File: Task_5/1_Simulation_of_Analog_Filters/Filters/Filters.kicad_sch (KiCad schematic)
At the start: 10 parts

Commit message: Work on 5.1
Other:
- note added: ".param R_HP=900*pI .param C_HP=1/(8100000*pI*pI)"
- note added: ".param R_LP=300*pI .param C_LP=1/(900000*pI*pI)"
- note added: ".param pI=3.14159 .param f_LP=1500 .param f_HP=4500 .param L=0.1"
- note added: "R_HP = 2*pI*L*f_LP C_HP = 1/(2*pI*R_HP*f_HP)"
- note added: "R_LP = 2*pI*L*f_LP C_LP = 1/(2*pI*R_LP*f_LP)"
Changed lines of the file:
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@@
+		)
+	)
+	(text "R_HP = 2*pI*L*f_LP\nC_HP = 1/(2*pI*R_HP*f_HP)"
+		(exclude_from_sim no)
+		(at 215.646 147.828 0)
+		(effects
+			(font
+				(size 1.27 1.27)
+			)
+		)
+	)
+	(text "R_LP = 2*pI*L*f_LP\nC_LP = 1/(2*pI*R_LP*f_LP)"
+		(exclude_from_sim no)
+		(at 139.7 147.32 0)
+		(effects
+			(font
+				(size 1.27 1.27)
+			)
 		)
 	)
@@
 		(exclude_from_sim no)
 		(at 139.7 44.45 0)
+		(effects
+			(font
+				(size 1.27 1.27)
+			)
+		)
+	)
+	(text ".param R_LP=300*pI\n.param C_LP=1/(900000*pI*pI)"
+		(exclude_from_sim no)
+		(at 139.446 156.464 0)
+		(effects
+			(font
+				(size 1.27 1.27)
+			)
+		)
+	)
+	(text ".param pI=3.14159\n.param f_LP=1500\n.param f_HP=4500\n.param L=0.1"
+		(exclude_from_sim no)
+		(at 261.874 83.058 0)
+		(effects
+			(font
+				(size 1.27 1.27)
+			)
+		)
+	)
+	(text ".param R_HP=900*pI\n.param C_HP=1/(8100000*pI*pI)"
+		(exclude_from_sim no)
+		(at 216.154 155.194 0)
 		(effects
 			(font
@@
 			)
 		)
-		(property "Sim.Params" "dc=0 ampl=1 f=1k ac=1"
+		(property "Sim.Params" "dc=0 ampl=1 f=5k ac=1"
 			(at 67.31 116.7101 0)
 			(effects

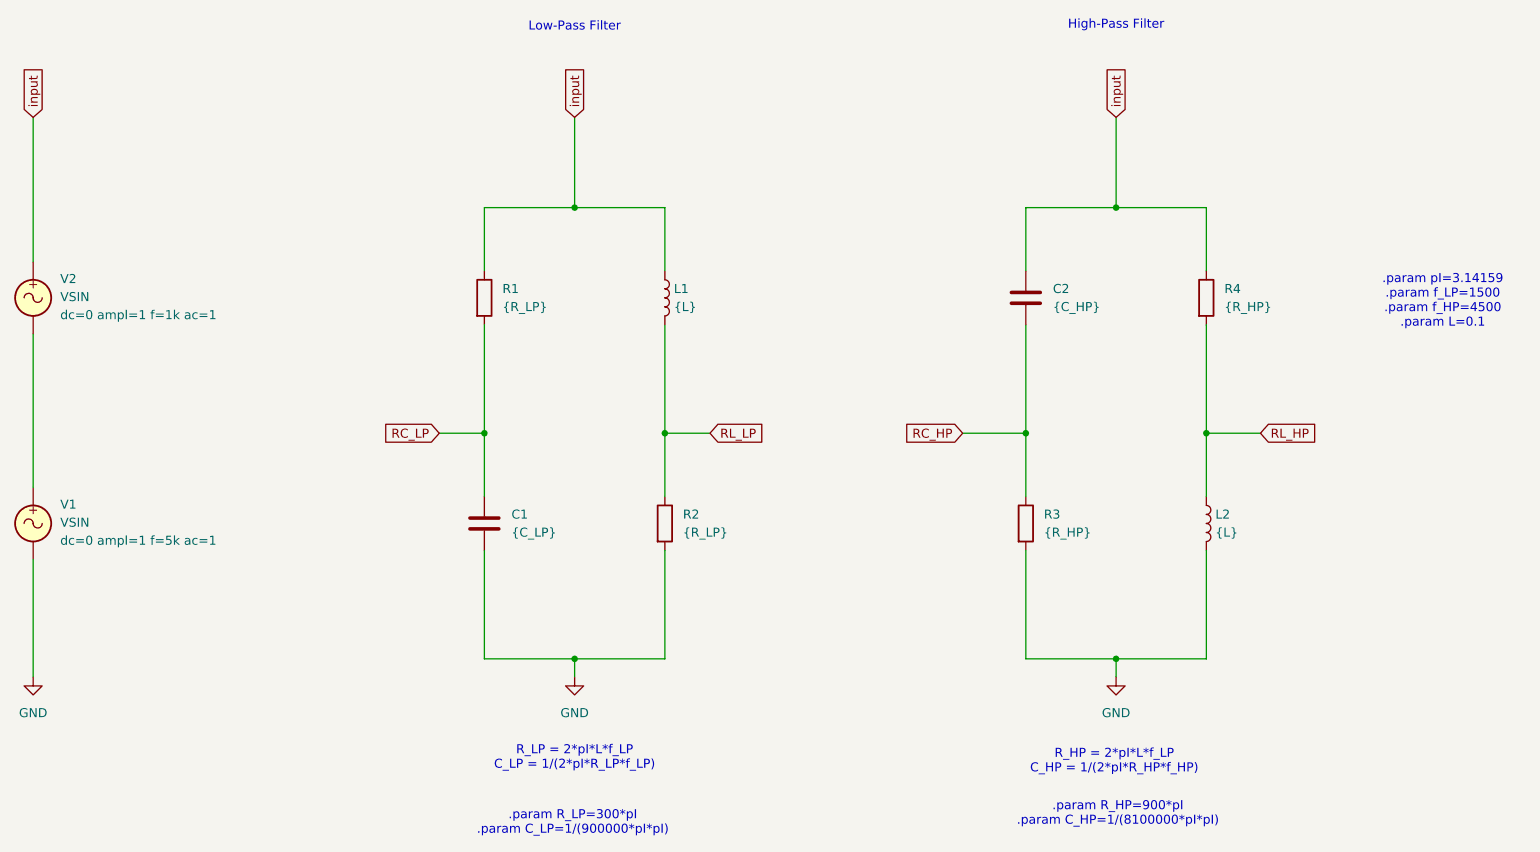
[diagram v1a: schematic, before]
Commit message: Ableiten von Bildern und daten für 5.1 und 5.3
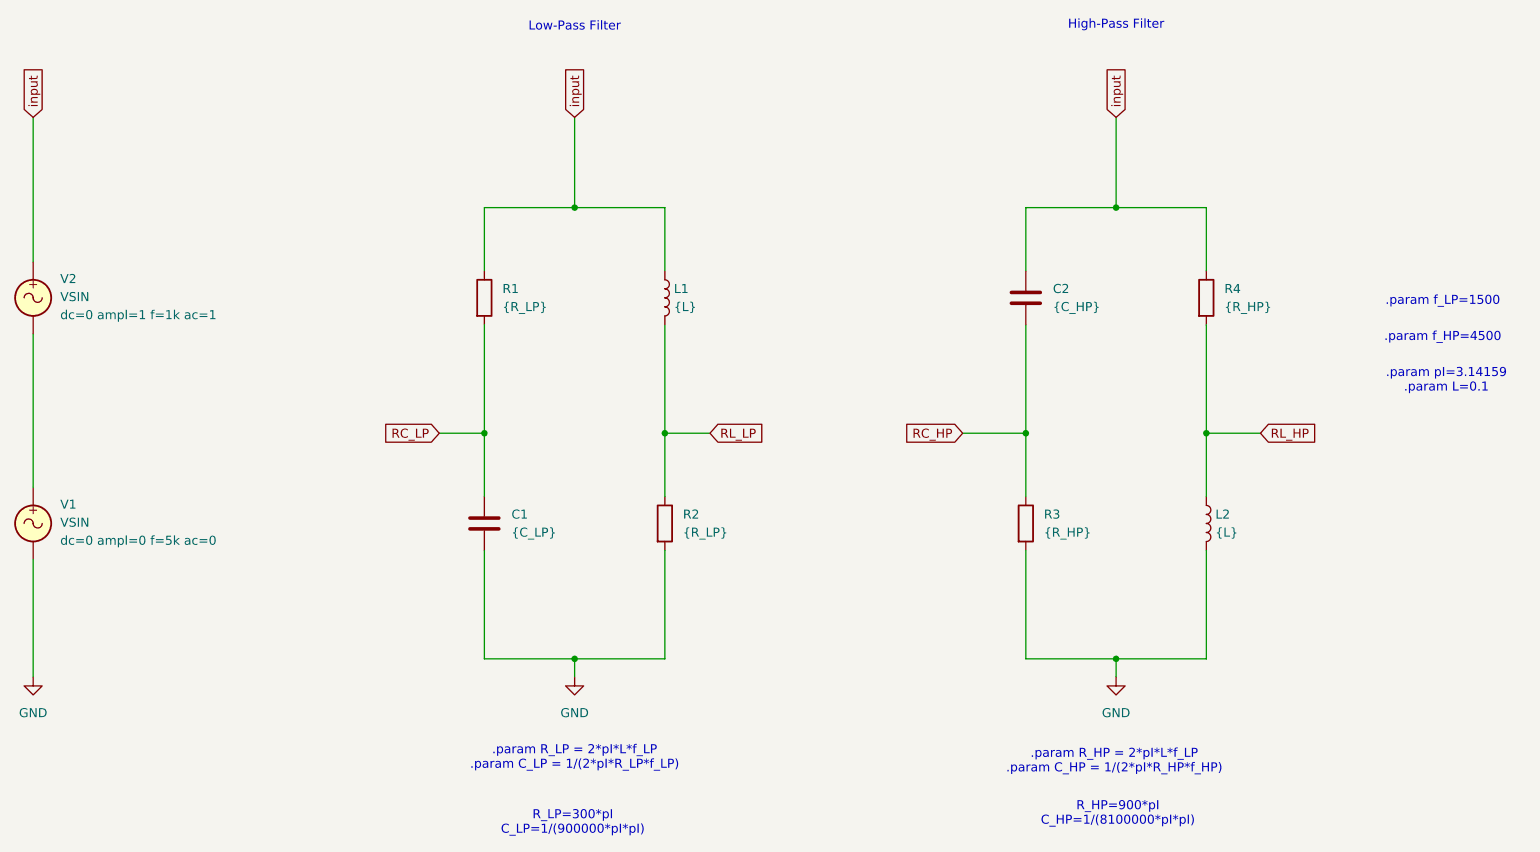
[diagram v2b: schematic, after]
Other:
- note added: ".param R_HP = 2*pI*L*f_LP .param C_HP = 1/(2*pI*R_HP*f_HP)"
- note added: ".param R_LP = 2*pI*L*f_LP .param C_LP = 1/(2*pI*R_LP*f_LP)"
- note added: ".param f_HP=4500"
- note added: ".param f_LP=1500"
- note added: ".param pI=3.14159 .param L=0.1"
- note added: "R_HP=900*pI C_HP=1/(8100000*pI*pI)"
- note added: "R_LP=300*pI C_LP=1/(900000*pI*pI)"
- note removed: ".param R_HP=900*pI .param C_HP=1/(8100000*pI*pI)"
- note removed: ".param R_LP=300*pI .param C_LP=1/(900000*pI*pI)"
- note removed: ".param pI=3.14159 .param f_LP=1500 .param f_HP=4500 .param L=0.1"
- note removed: "R_HP = 2*pI*L*f_LP C_HP = 1/(2*pI*R_HP*f_HP)"
- note removed: "R_LP = 2*pI*L*f_LP C_LP = 1/(2*pI*R_LP*f_LP)"
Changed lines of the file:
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@@
 		)
 	)
-	(text "R_HP = 2*pI*L*f_LP\nC_HP = 1/(2*pI*R_HP*f_HP)"
+	(text ".param pI=3.14159\n.param L=0.1"
+		(exclude_from_sim no)
+		(at 262.382 94.234 0)
+		(effects
+			(font
+				(size 1.27 1.27)
+			)
+		)
+	)
+	(text ".param R_HP = 2*pI*L*f_LP\n.param C_HP = 1/(2*pI*R_HP*f_HP)"
 		(exclude_from_sim no)
 		(at 215.646 147.828 0)
@@
 		)
 	)
-	(text "R_LP = 2*pI*L*f_LP\nC_LP = 1/(2*pI*R_LP*f_LP)"
+	(text ".param R_LP = 2*pI*L*f_LP\n.param C_LP = 1/(2*pI*R_LP*f_LP)"
 		(exclude_from_sim no)
 		(at 139.7 147.32 0)
@@
 		)
 	)
-	(text ".param R_LP=300*pI\n.param C_LP=1/(900000*pI*pI)"
+	(text "R_LP=300*pI\nC_LP=1/(900000*pI*pI)"
 		(exclude_from_sim no)
 		(at 139.446 156.464 0)
@@
 		)
 	)
-	(text ".param pI=3.14159\n.param f_LP=1500\n.param f_HP=4500\n.param L=0.1"
+	(text ".param f_HP=4500"
+		(exclude_from_sim no)
+		(at 261.874 88.138 0)
+		(effects
+			(font
+				(size 1.27 1.27)
+			)
+		)
+	)
+	(text ".param f_LP=1500"
 		(exclude_from_sim no)
 		(at 261.874 83.058 0)
@@
 		)
 	)
-	(text ".param R_HP=900*pI\n.param C_HP=1/(8100000*pI*pI)"
+	(text "R_HP=900*pI\nC_HP=1/(8100000*pI*pI)"
 		(exclude_from_sim no)
 		(at 216.154 155.194 0)
@@
 			)
 		)
-		(property "Sim.Params" "dc=0 ampl=1 f=5k ac=1"
+		(property "Sim.Params" "dc=0 ampl=0 f=5k ac=0"
 			(at 67.31 116.7101 0)
 			(effects

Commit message: More work done
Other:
- note added: ".param R_HP = 2*pI*L*f_HP .param C_HP = 1/(2*pI*R_HP*f_HP)"
- note removed: ".param R_HP = 2*pI*L*f_LP .param C_HP = 1/(2*pI*R_HP*f_HP)"
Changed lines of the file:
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@@
 		)
 	)
-	(text ".param R_HP = 2*pI*L*f_LP\n.param C_HP = 1/(2*pI*R_HP*f_HP)"
+	(text ".param R_HP = 2*pI*L*f_HP\n.param C_HP = 1/(2*pI*R_HP*f_HP)"
 		(exclude_from_sim no)
 		(at 215.646 147.828 0)
@@
 			)
 		)
-		(property "Sim.Params" "dc=0 ampl=0 f=5k ac=0"
+		(property "Sim.Params" "dc=0 ampl=1 f=5k ac=1"
 			(at 67.31 116.7101 0)
 			(effects
